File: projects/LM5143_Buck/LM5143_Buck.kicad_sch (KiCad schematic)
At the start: 120 parts, among them J1 Bat In, J2 24V Out, J3 I2C Socket, J4 I2C Socket, Q1 IGC025S08S1, Q2 IGC025S08S1, Q3 IGC025S08S1, Q4 IGC025S08S1, SW1 SW_SPDT, SW2 SW_SPDT, SW3 Addr_Switch, SW4 Addr_Switch, U2 LM5113-Q1, U3 LM5113-Q1, U4 AP7387-50FDC-7, U5 TLV74033, U6 INA226

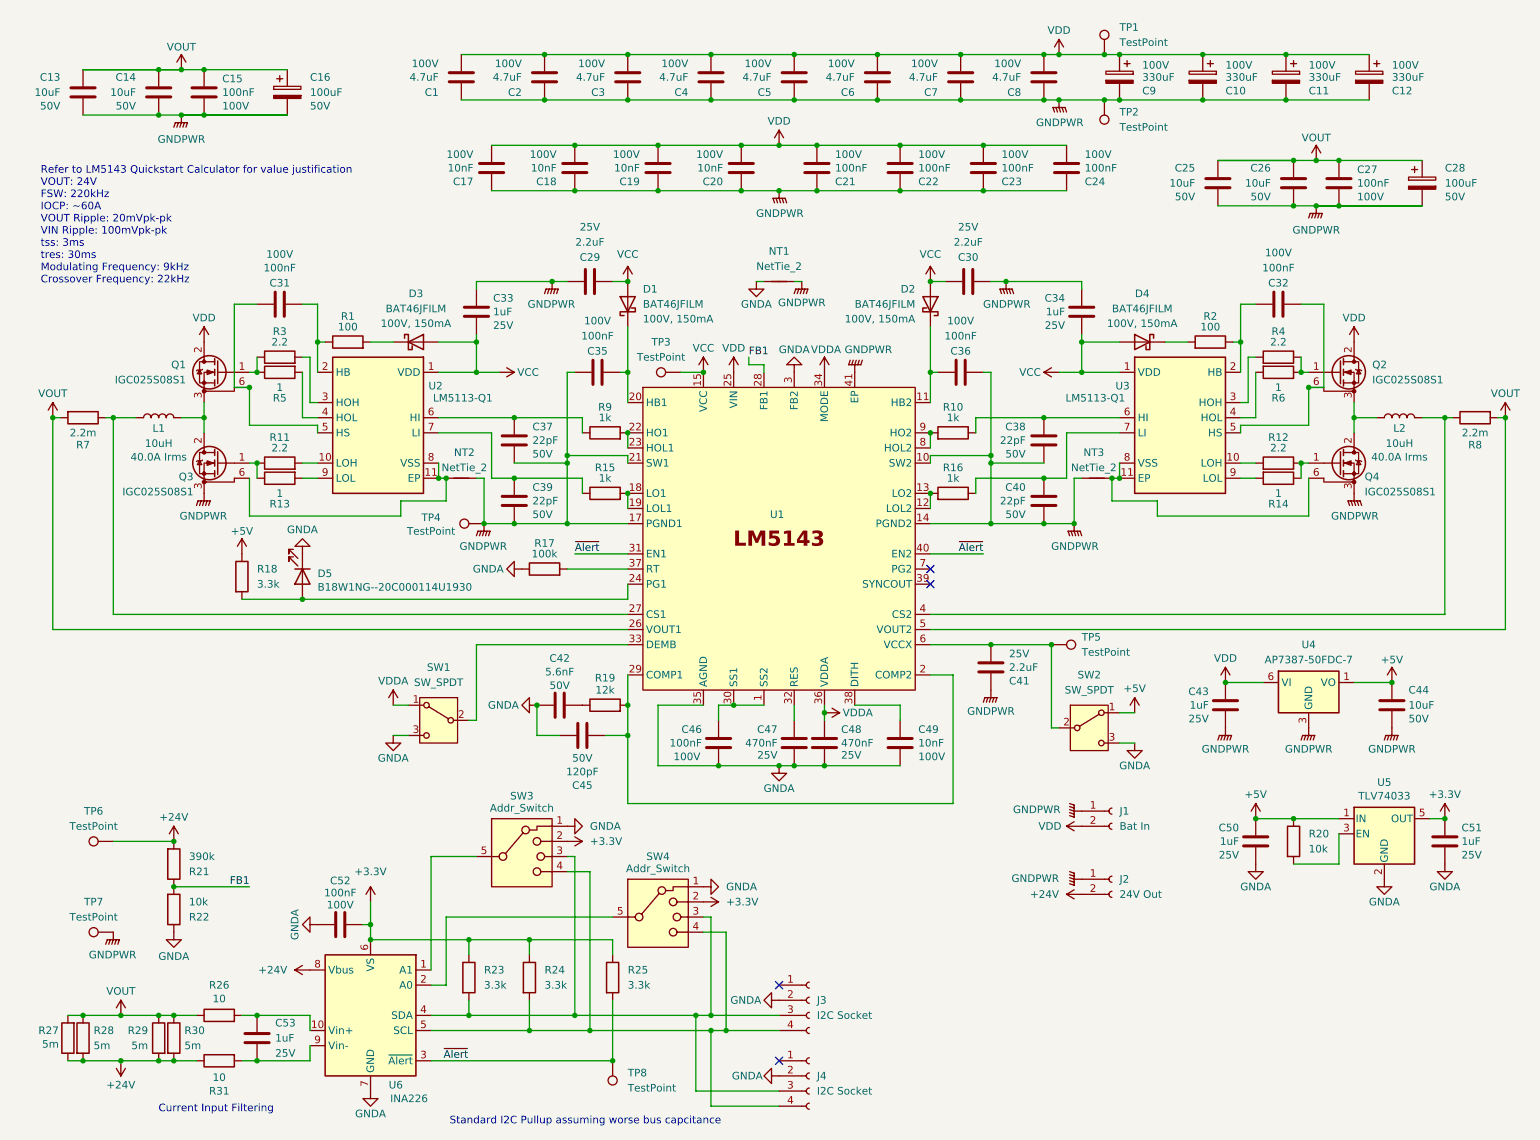
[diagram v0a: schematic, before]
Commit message: Schematic update and partial routing
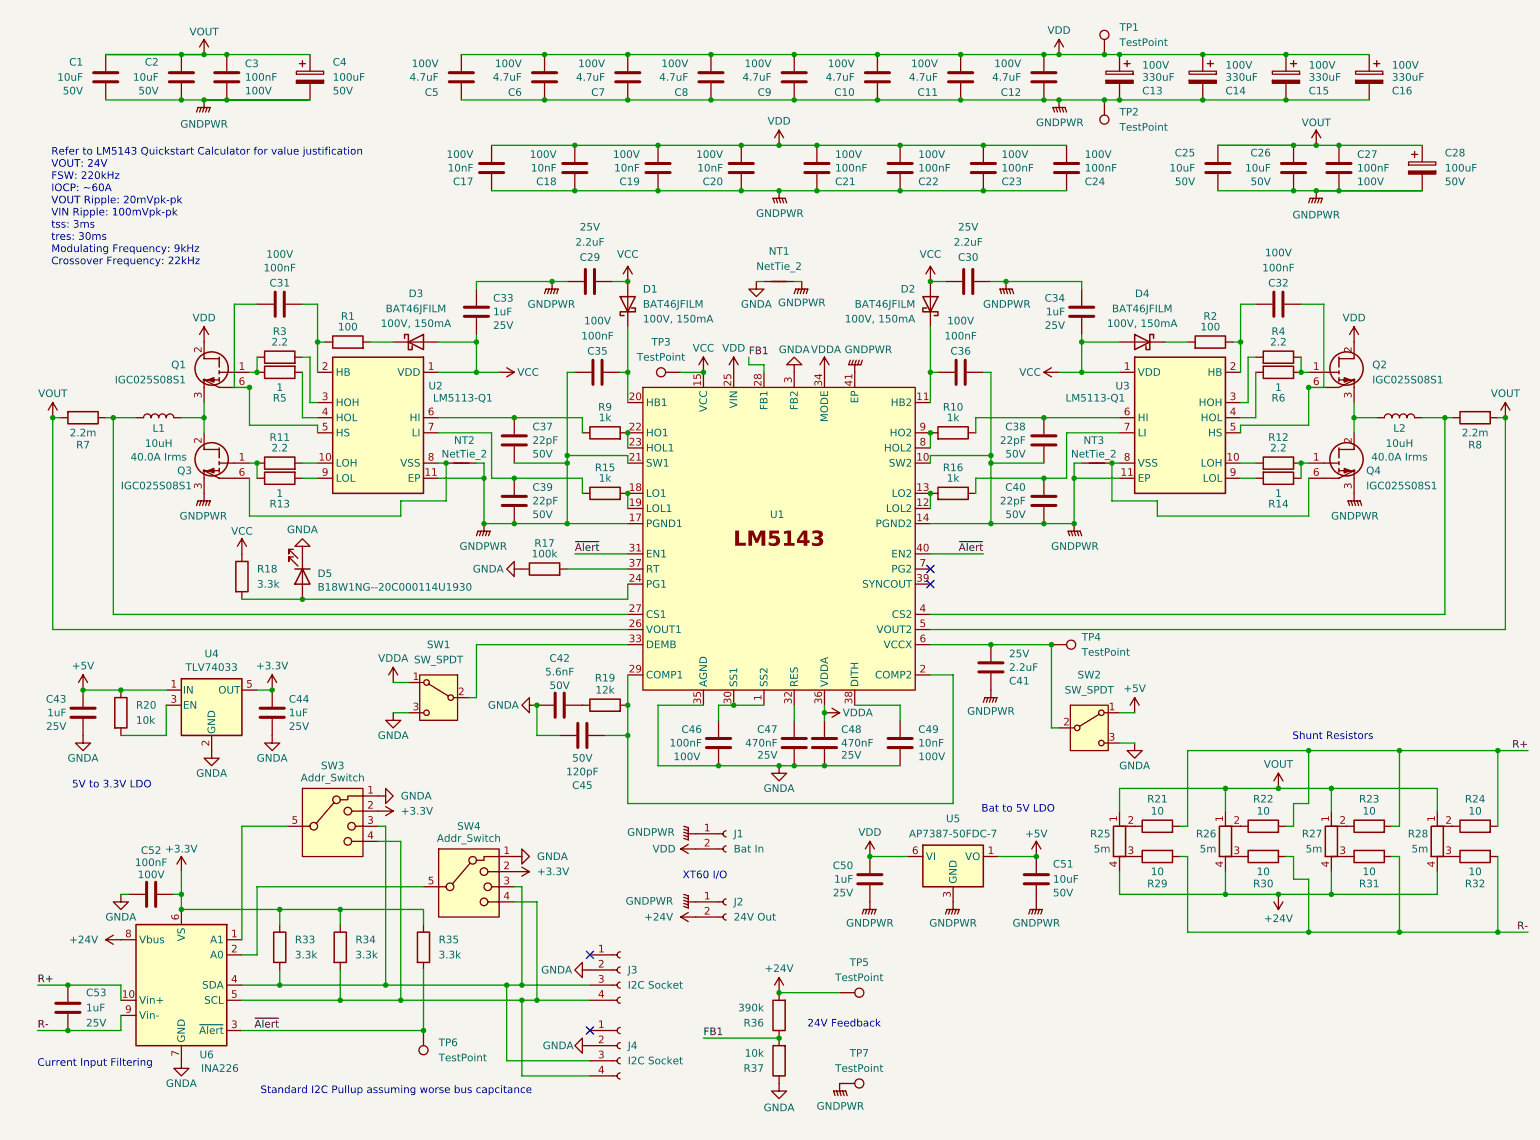
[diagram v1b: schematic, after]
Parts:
- removed Q2, Q3, Q4: IGC025S08S1, footprints:PG‑TSON‑6, symbol Transistor_FET:Q_NMOS_GSSD
- removed R26: 10, Resistor_SMD:R_0603_1608Metric, symbol Device:R
- removed R27: 5m, footprints:PCSR2512_Alt, symbol Device:R
- removed R28: 5m, footprints:PCSR2512_Alt_2, symbol Device:R
- removed TP4: TestPoint, TestPoint:TestPoint_Keystone_5000-5004_Miniature, symbol Connector:TestPoint
- added Q2, Q3, Q4: IGC025S08S1, footprints:PG‑TSON‑6, symbol Transistor_FET:GS66508B
- added R21, R22, R23, R24, R32: 10, Resistor_SMD:R_0603_1608Metric, symbol Device:R
- added R25, R26, R27, R28: 5m, footprints:PCSR2512, symbol Device:R_Shunt
- Q1: symbol Transistor_FET:Q_NMOS_GSSD -> Transistor_FET:GS66508B
- R29: value 5m -> 10; footprint footprints:PCSR2512_Alt_2 -> Resistor_SMD:R_0603_1608Metric
- R30: value 5m -> 10; footprint footprints:PCSR2512_Alt -> Resistor_SMD:R_0603_1608Metric
- TP3: footprint TestPoint:TestPoint_Keystone_5000-5004_Miniature -> TestPoint:TestPoint_Pad_D2.0mm
- U2, U3: footprint Package_SON:WSON-10-1EP_4x4mm_P0.8mm_EP2.6x3mm_ThermalVias -> footprints:WSON-10-1EP_4x4mm_P0.8mm_EP2.6x3mm_ThermalVias
- renumbered C13 to C1, C6 to C10, C7 to C11, C8 to C12, C9 to C13, C10 to C14, C11 to C15, C12 to C16, C14 to C2, C15 to C3, C16 to C4, C50 to C43, C51 to C44, C1 to C5, C43 to C50, C44 to C51, C2 to C6, C3 to C7, C4 to C8, C5 to C9, R23 to R33, R24 to R34, R25 to R35, R21 to R36, R22 to R37, TP5 to TP4, TP6 to TP5, TP8 to TP6, U5 to U4, U4 to U5
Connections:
- net +24V: now also R25.4, R26.4, R27.4, R28.4; no longer R29.2, R30.2, R31.1
- net +5V: no longer R18.1
- net GND: now also U2.11 (EP), U3.11 (EP), Q3.3 (S), Q3.5 (S), Q4.3 (S), Q4.5 (S)
- net VCC: now also R18.1
- net VDD: now also Q2.2 (D), Q2.4 (D)
- net VOUT: now also R25.1, R26.1, R27.1, R28.1; no longer R29.1, R30.1
- net at R8.1, U1.4 (CS2): now also L2.2; no longer L2.1
- net at L1.2, Q1.3 (S), Q1.5 (S): now also Q3.2 (D), Q3.4 (D)
- net at R11.1, R13.1: now also Q3.1 (G)
- net at R4.1, R6.1: now also Q2.1 (G)
- net at C32.1, U3.5 (HS): now also Q2.6 (SS)
- net R+: now reaches C53.1, U6.10 (Vin+)
- net R+: now also R21.2, R22.2, R23.2, R24.2
- net R-: now reaches C53.2, R31.2, U6.9 (Vin-)
- net R-: now also R29.2, R30.2, R32.2
- net at NT2.1, U2.8 (VSS): now also Q3.6 (SS); no longer U2.11 (EP)
- net at NT3.1, U3.8 (VSS): now also Q4.6 (SS); no longer U3.11 (EP)
- net at R12.1, R14.1: now also Q4.1 (G)
- new net: R21.1, R25.2
- new net: R24.1, R28.2
- new net: R22.1, R26.2
- new net: R26.3, R30.1
- new net: R28.3, R32.1
- new net: R23.1, R27.2
- new net: R27.3, R31.1
- new net: R25.3, R29.1
- new net: L2.1, Q2.3 (S), Q2.5 (S), Q4.2 (D), Q4.4 (D)
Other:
- note added: "24V Feedback"
- note added: "5V to 3.3V LDO"
- note added: "Bat to 5V LDO"
- note added: "Shunt Resistors"
- note added: "XT60 I/O"
- moved on the sheet: C1, C2, C25, C26, C27, C28, C3, C4, C43, C44, C50, C51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

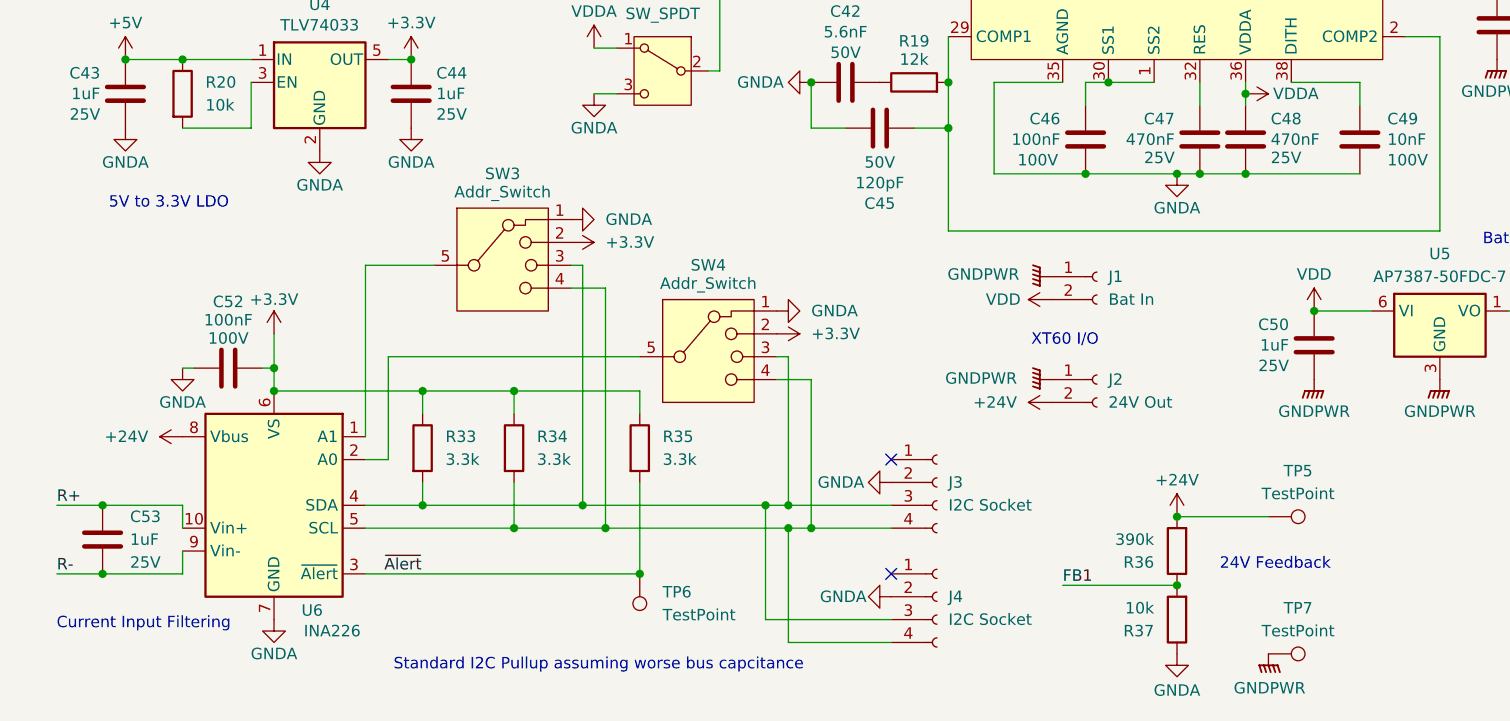
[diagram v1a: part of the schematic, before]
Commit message: Fully routed, no via stitching yet
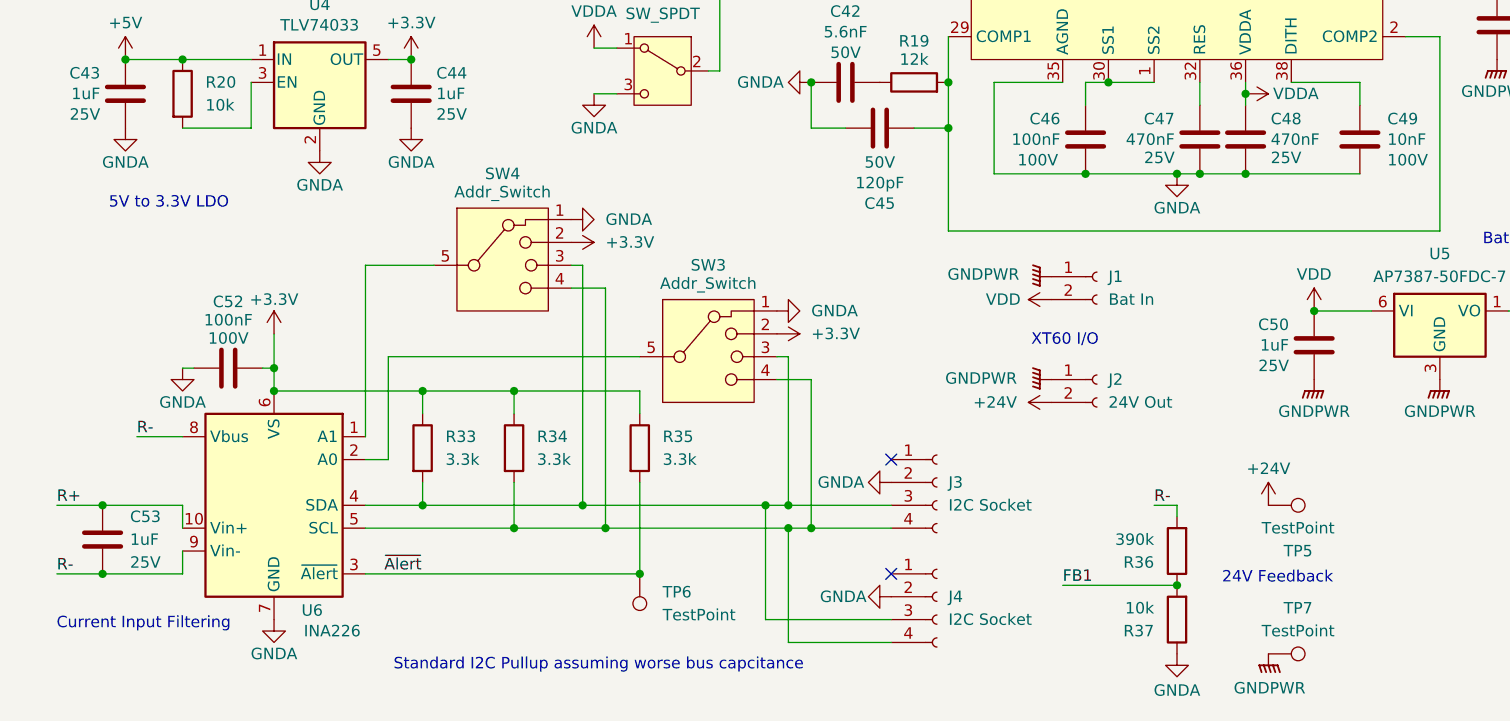
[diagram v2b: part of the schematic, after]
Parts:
- renumbered SW4 to SW3, SW3 to SW4
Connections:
- net +24V: no longer R36.2, U6.8 (Vbus)
- net R-: now also R36.2, U6.8 (Vbus)
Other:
- moved on the sheet: TP5
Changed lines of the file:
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@@
 	(text "24V Feedback"
 		(exclude_from_sim no)
-		(at 150.622 184.404 0)
+		(at 150.876 185.928 0)
 		(effects
 			(font
@@
 	)
 	(junction
-		(at 139.7 179.07)
-		(diameter 0)
-		(color 0 0 0 0)
-	)
-	(junction
 		(at 260.35 138.43)
 		(diameter 0)
@@
 	(wire
 		(pts
+			(xy 139.7 177.8) (xy 139.7 179.07)
+		)
+		(stroke
+			(width 0)
+			(type default)
+		)
+	)
+	(wire
+		(pts
 			(xy 134.62 72.39) (xy 134.62 73.66)
 		)
@@
 	(wire
 		(pts
+			(xy 29.21 170.18) (xy 24.13 170.18)
+		)
+		(stroke
+			(width 0)
+			(type default)
+		)
+	)
+	(wire
+		(pts
 			(xy 29.21 185.42) (xy 20.32 185.42)
 		)
@@
 	(wire
 		(pts
+			(xy 139.7 177.8) (xy 137.16 177.8)
+		)
+		(stroke
+			(width 0)
+			(type default)
+		)
+	)
+	(wire
+		(pts
 			(xy 223.52 162.56) (xy 232.41 162.56)
 		)
@@
 	(wire
 		(pts
-			(xy 149.86 179.07) (xy 139.7 179.07)
-		)
-		(stroke
-			(width 0)
-			(type default)
-		)
-	)
-	(wire
-		(pts
 			(xy 119.38 36.83) (xy 133.35 36.83)
 		)
@@
 		)
 	)
+	(label "R-"
+		(at 137.16 177.8 0)
+		(effects
+			(font
+				(size 1.27 1.27)
+			)
+			(justify left bottom)
+		)
+	)
 	(label "R+"
 		(at 265.43 138.43 180)
@@
 		)
 	)
+	(label "R-"
+		(at 24.13 170.18 0)
+		(effects
+			(font
+				(size 1.27 1.27)
+			)
+			(justify left bottom)
+		)
+	)
 	(label "~{Alert}"
 		(at 55.7683 185.42 180)
@@
 		(on_board yes)
 		(dnp no)
-		(property "Reference" "SW4"
+		(property "Reference" "SW3"
 			(at 87.63 151.13 0)
 			(effects
@@
 			(project ""
 				(path "/80c4af3d-2f3c-4656-872e-20096fd9d2a6"
-					(reference "SW4")
+					(reference "SW3")
 					(unit 1)
 				)
@@
 			)
 		)
-		(property "Datasheet" "https://www.lcsc.com/product-detail/C109318.html"
+		(property "Datasheet" "https://www.lcsc.com/product-detail/C861082.html"
 			(at 203.2 151.13 0)
 			(effects
@@
 			)
 		)
-		(property "Datasheet" "https://www.lcsc.com/product-detail/C109318.html"
+		(property "Datasheet" "https://www.lcsc.com/product-detail/C861082.html"
 			(at 256.54 151.13 0)
 			(effects
@@
 			)
 		)
-		(property "Datasheet" "https://www.lcsc.com/product-detail/C109318.html"
+		(property "Datasheet" "https://www.lcsc.com/product-detail/C861082.html"
 			(at 220.98 151.13 0)
 			(effects
@@
 	(symbol
 		(lib_id "power:+24V")
-		(at 139.7 179.07 0)
+		(at 149.86 177.8 0)
 		(unit 1)
 		(exclude_from_sim no)
@@
 		(dnp no)
 		(property "Reference" "#PWR065"
-			(at 139.7 182.88 0)
+			(at 149.86 181.61 0)
 			(effects
 				(font
@@
 		)
 		(property "Value" "+24V"
-			(at 139.7 175.006 0)
+			(at 149.86 173.736 0)
 			(effects
 				(font
@@
 		)
 		(property "Footprint" ""
-			(at 139.7 179.07 0)
+			(at 149.86 177.8 0)
 			(effects
 				(font
@@
 		)
 		(property "Datasheet" ""
-			(at 139.7 179.07 0)
+			(at 149.86 177.8 0)
 			(effects
 				(font
@@
 		)
 		(property "Description" "Power symbol creates a global label with name \"+24V\""
-			(at 139.7 179.07 0)
+			(at 149.86 177.8 0)
 			(effects
 				(font
@@
 		(on_board yes)
 		(dnp no)
-		(property "Reference" "SW3"
+		(property "Reference" "SW4"
 			(at 64.77 140.97 0)
 			(effects
@@
 			(project "LM5143_Buck"
 				(path "/80c4af3d-2f3c-4656-872e-20096fd9d2a6"
-					(reference "SW3")
+					(reference "SW4")
 					(unit 1)
 				)
@@
 			)
 		)
-		(property "Datasheet" "https://www.lcsc.com/product-detail/C109318.html"
+		(property "Datasheet" "https://www.lcsc.com/product-detail/C861082.html"
 			(at 220.98 156.21 0)
 			(effects
@@
 			)
 		)
-		(property "Datasheet" "https://www.lcsc.com/product-detail/C109318.html"
+		(property "Datasheet" "https://www.lcsc.com/product-detail/C861082.html"
 			(at 256.54 156.21 0)
 			(effects
@@
 			)
 		)
-		(property "Datasheet" "https://www.lcsc.com/product-detail/C109318.html"
+		(property "Datasheet" "https://www.lcsc.com/product-detail/C861082.html"
 			(at 238.76 151.13 0)
 			(effects
@@
 	)
 	(symbol
-		(lib_id "power:+24V")
-		(at 29.21 170.18 90)
-		(unit 1)
-		(exclude_from_sim no)
-		(in_bom yes)
-		(on_board yes)
-		(dnp no)
-		(fields_autoplaced yes)
-		(property "Reference" "#PWR063"
-			(at 33.02 170.18 0)
-			(effects
-				(font
-					(size 1.27 1.27)
-				)
-				(hide yes)
-			)
-		)
-		(property "Value" "+24V"
-			(at 25.4 170.1799 90)
-			(effects
-				(font
-					(size 1.27 1.27)
-				)
-				(justify left)
-			)
-		)
-		(property "Footprint" ""
-			(at 29.21 170.18 0)
-			(effects
-				(font
-					(size 1.27 1.27)
-				)
-				(hide yes)
-			)
-		)
-		(property "Datasheet" ""
-			(at 29.21 170.18 0)
-			(effects
-				(font
-					(size 1.27 1.27)
-				)
-				(hide yes)
-			)
-		)
-		(property "Description" "Power symbol creates a global label with name \"+24V\""
-			(at 29.21 170.18 0)
-			(effects
-				(font
-					(size 1.27 1.27)
-				)
-				(hide yes)
-			)
-		)
-		(pin "1"
-		)
-		(instances
-			(project "LM5143_Buck"
-				(path "/80c4af3d-2f3c-4656-872e-20096fd9d2a6"
-					(reference "#PWR063")
-					(unit 1)
-				)
-			)
-		)
-	)
-	(symbol
 		(lib_id "Device:R_Shunt")
 		(at 232.41 153.67 0)
@@
 			)
 		)
-		(property "Datasheet" "https://www.lcsc.com/product-detail/C109318.html"
+		(property "Datasheet" "https://www.lcsc.com/product-detail/C861082.html"
 			(at 203.2 156.21 0)
 			(effects
@@
 			)
 		)
-		(property "Datasheet" "https://www.lcsc.com/product-detail/C109318.html"
+		(property "Datasheet" "https://www.lcsc.com/product-detail/C861082.html"
 			(at 238.76 156.21 0)
 			(effects
@@
 	(symbol
 		(lib_id "Connector:TestPoint")
-		(at 149.86 179.07 270)
-		(mirror x)
+		(at 149.86 177.8 270)
 		(unit 1)
 		(exclude_from_sim no)
@@
 		(on_board yes)
 		(dnp no)
-		(fields_autoplaced yes)
 		(property "Reference" "TP5"
-			(at 153.162 173.99 90)
+			(at 153.162 182.88 90)
 			(effects
 				(font
@@
 		)
 		(property "Value" "TestPoint"
-			(at 153.162 176.53 90)
+			(at 153.162 180.34 90)
 			(effects
 				(font
@@
 		)
 		(property "Footprint" "TestPoint:TestPoint_Keystone_5000-5004_Miniature"
-			(at 149.86 173.99 0)
+			(at 149.86 182.88 0)
 			(effects
 				(font
@@
 		)
 		(property "Datasheet" "https://www.lcsc.com/product-detail/C5199801.html"
-			(at 149.86 173.99 0)
+			(at 149.86 182.88 0)
 			(effects
 				(font
@@
 		)
 		(property "Description" "test point"
-			(at 149.86 179.07 0)
+			(at 149.86 177.8 0)
 			(effects
 				(font
